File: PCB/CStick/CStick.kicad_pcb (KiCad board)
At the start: 2 copper layers, 39.1 x 31.5 mm, 6 parts, among them J1 Conn_01x04_Male, U1 Stickbox_Assembly

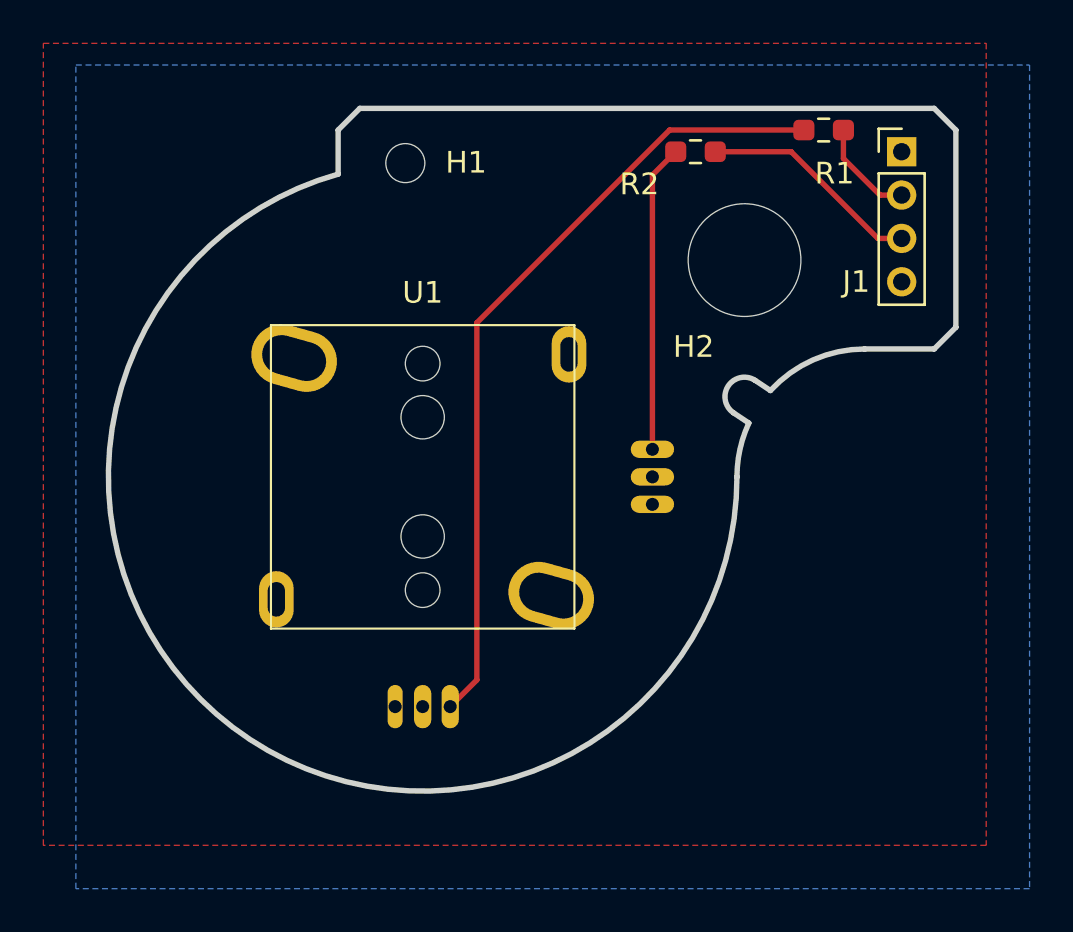
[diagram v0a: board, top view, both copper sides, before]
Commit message: Updated the c-stick board, connector was flipped
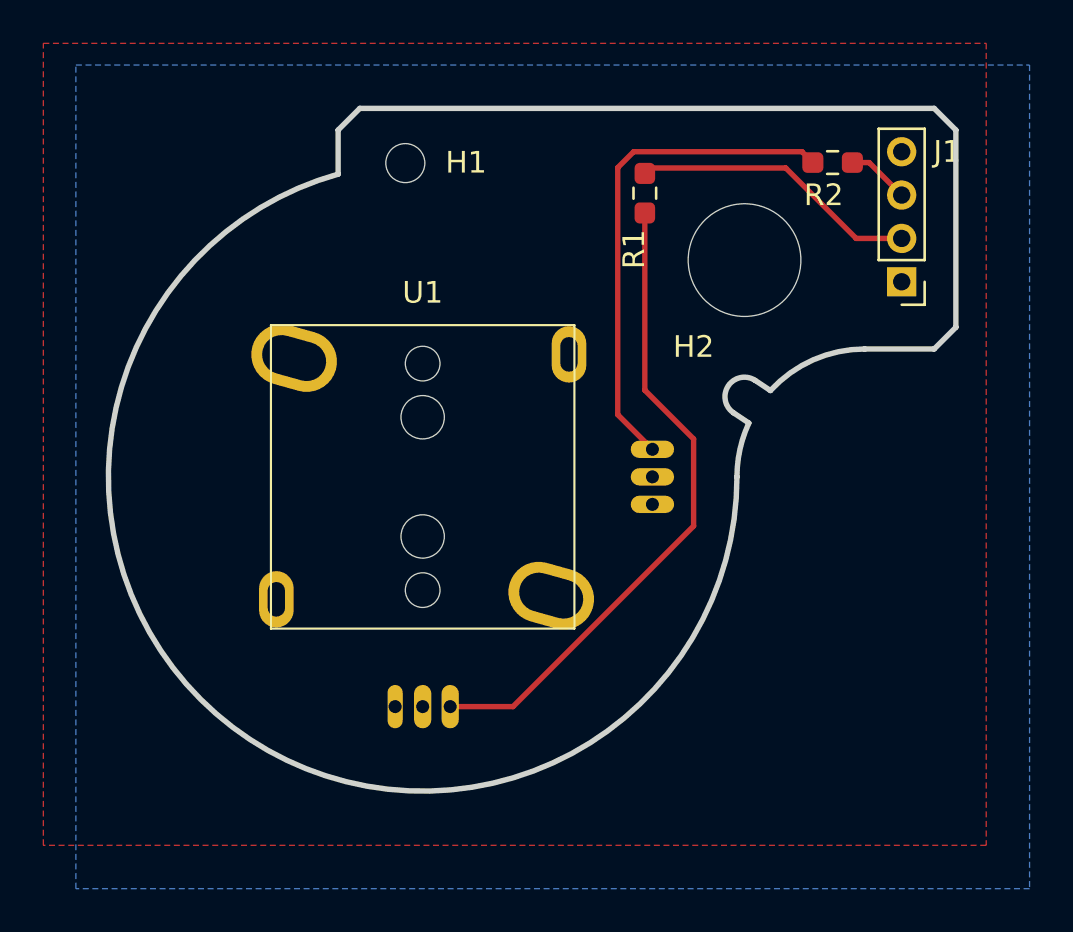
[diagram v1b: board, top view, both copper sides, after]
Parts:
- moved R1 8.75 mm to (160.2, 86.9), turned to -90 degrees
- moved R2 6.34 mm to (168.9, 85.5)
- moved J1 6.00 mm to (172.1, 91.0), turned to 180 degrees
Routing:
- net Net-(R2-Pad2): track 14.2 -> 23.2 mm
- net Net-(J1-Pad2): track 4.70 -> 13.3 mm
- net Net-(J1-Pad3): track 10.3 -> 2.90 mm
- net Net-(R1-Pad2): track 37.0 -> 30.1 mm
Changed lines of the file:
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@@
 (kicad_pcb (version 20211014) (generator pcbnew)
   (general
-    (thickness 1.6)
+    (thickness 1.59)
   )
   (paper "A4")
@@
     (0 "F.Cu" signal)
     (31 "B.Cu" signal)
-    (35 "F.Paste" user)
+    (36 "B.SilkS" user "B.Silkscreen")
     (37 "F.SilkS" user "F.Silkscreen")
+    (38 "B.Mask" user)
     (39 "F.Mask" user)
     (40 "Dwgs.User" user "User.Drawings")
+    (41 "Cmts.User" user "User.Comments")
     (44 "Edge.Cuts" user)
     (45 "Margin" user)
     (46 "B.CrtYd" user "B.Courtyard")
     (47 "F.CrtYd" user "F.Courtyard")
-    (49 "F.Fab" user)
   )
   (setup
@@
       (layer "dielectric 1" (type "core") (thickness 1.51) (material "FR4") (epsilon_r 4.5) (loss_tangent 0.02))
       (layer "B.Cu" (type "copper") (thickness 0.035))
-      (layer "B.Mask" (type "Bottom Solder Mask") (thickness 0.01))
       (copper_finish "None")
       (dielectric_constraints no)
@@
   (net 6 "Net-(R2-Pad2)")
   (footprint "Resistor_SMD:R_0603_1608Metric_Pad0.98x0.95mm_HandSolder" (layer "F.Cu")
-    (at 168.5 84 180)
+    (at 160.25 86.9125 -90)
     (descr "Resistor SMD 0603 (1608 Metric), square (rectangular) end terminal, IPC_7351 nominal with elongated pad for handsoldering. (Body size source: IPC-SM-782 page 72, https://www.pcb-3d.com/wordpress/wp-content/uploads/ipc-sm-782a_amendment_1_and_2.pdf), generated with kicad-footprint-generator")
     (tags "resistor handsolder")
@@
     (property "Sheetname" "")
     (attr smd)
-    (fp_text reference "R1" (at -0.5 -2) (layer "F.SilkS")
-      (effects (font (size 1 1) (thickness 0.15)))
-    )
-    (fp_text value "10k" (at 0 1.43) (layer "F.Fab")
-      (effects (font (size 1 1) (thickness 0.15)))
-    )
-    (fp_text user "${REFERENCE}" (at 0 0) (layer "F.Fab")
+    (fp_text reference "R1" (at 2.5875 0.5 90) (layer "F.SilkS")
+      (effects (font (size 1 1) (thickness 0.15)))
+    )
+    (fp_text value "10k" (at 0 1.43 90) (layer "F.Fab")
+      (effects (font (size 1 1) (thickness 0.15)))
+    )
+    (fp_text user "${REFERENCE}" (at 0 0 90) (layer "F.Fab")
       (effects (font (size 0.4 0.4) (thickness 0.06)))
     )
@@
     (fp_line (start -0.8 0.4125) (end -0.8 -0.4125) (layer "F.Fab") (width 0.1))
     (fp_line (start 0.8 -0.4125) (end 0.8 0.4125) (layer "F.Fab") (width 0.1))
-    (pad "1" smd roundrect (at -0.9125 0 180) (size 0.975 0.95) (layers "F.Cu" "F.Paste" "F.Mask") (roundrect_rratio 0.25)
+    (pad "1" smd roundrect (at -0.9125 0 270) (size 0.975 0.95) (layers "F.Cu" "F.Paste" "F.Mask") (roundrect_rratio 0.25)
       (net 3 "Net-(J1-Pad2)") (pintype "passive"))
-    (pad "2" smd roundrect (at 0.9125 0 180) (size 0.975 0.95) (layers "F.Cu" "F.Paste" "F.Mask") (roundrect_rratio 0.25)
+    (pad "2" smd roundrect (at 0.9125 0 270) (size 0.975 0.95) (layers "F.Cu" "F.Paste" "F.Mask") (roundrect_rratio 0.25)
       (net 5 "Net-(R1-Pad2)") (pintype "passive"))
     (model "${KICAD6_3DMODEL_DIR}/Resistor_SMD.3dshapes/R_0603_1608Metric.wrl"
@@
   )
   (footprint "Resistor_SMD:R_0603_1608Metric_Pad0.98x0.95mm_HandSolder" (layer "F.Cu")
-    (at 162.5875 85 180)
+    (at 168.9125 85.5 180)
     (descr "Resistor SMD 0603 (1608 Metric), square (rectangular) end terminal, IPC_7351 nominal with elongated pad for handsoldering. (Body size source: IPC-SM-782 page 72, https://www.pcb-3d.com/wordpress/wp-content/uploads/ipc-sm-782a_amendment_1_and_2.pdf), generated with kicad-footprint-generator")
     (tags "resistor handsolder")
@@
     (property "Sheetname" "")
     (attr smd)
-    (fp_text reference "R2" (at 2.5875 -1.5) (layer "F.SilkS")
+    (fp_text reference "R2" (at 0.4125 -1.5) (layer "F.SilkS")
       (effects (font (size 1 1) (thickness 0.15)))
     )
@@
   )
   (footprint "Connector_PinHeader_2.00mm:PinHeader_1x04_P2.00mm_Vertical" (layer "F.Cu")
-    (at 172.1 85)
+    (at 172.1 91 180)
     (descr "Through hole straight pin header, 1x04, 2.00mm pitch, single row")
     (tags "Through hole pin header THT 1x04 2.00mm single row")
@@
     (fp_line (start -0.5 -1) (end 1 -1) (layer "F.Fab") (width 0.1))
     (fp_line (start -1 -0.5) (end -0.5 -1) (layer "F.Fab") (width 0.1))
-    (pad "1" thru_hole rect (at 0 0) (size 1.35 1.35) (drill 0.8) (layers *.Cu *.Mask)
+    (pad "1" thru_hole rect (at 0 0 180) (size 1.35 1.35) (drill 0.8) (layers *.Cu *.Mask)
       (net 1 "VCC") (pinfunction "Pin_1") (pintype "passive"))
-    (pad "2" thru_hole oval (at 0 2) (size 1.35 1.35) (drill 0.8) (layers *.Cu *.Mask)
+    (pad "2" thru_hole oval (at 0 2 180) (size 1.35 1.35) (drill 0.8) (layers *.Cu *.Mask)
       (net 3 "Net-(J1-Pad2)") (pinfunction "Pin_2") (pintype "passive"))
-    (pad "3" thru_hole oval (at 0 4) (size 1.35 1.35) (drill 0.8) (layers *.Cu *.Mask)
+    (pad "3" thru_hole oval (at 0 4 180) (size 1.35 1.35) (drill 0.8) (layers *.Cu *.Mask)
       (net 4 "Net-(J1-Pad3)") (pinfunction "Pin_3") (pintype "passive"))
-    (pad "4" thru_hole oval (at 0 6) (size 1.35 1.35) (drill 0.8) (layers *.Cu *.Mask)
+    (pad "4" thru_hole oval (at 0 6 180) (size 1.35 1.35) (drill 0.8) (layers *.Cu *.Mask)
       (net 2 "GND") (pinfunction "Pin_4") (pintype "passive"))
     (model "${KICAD6_3DMODEL_DIR}/Connector_PinHeader_2.00mm.3dshapes/PinHeader_1x04_P2.00mm_Vertical.wrl"
@@
   (gr_line (start 146.1 84) (end 146.1 86.034328) (layer "Edge.Cuts") (width 0.25))
   (gr_line (start 174.6 93.1) (end 174.6 84) (layer "Edge.Cuts") (width 0.25))
-  (segment (start 171.1 87) (end 169.4125 85.3125) (width 0.25) (layer "F.Cu") (net 3))
-  (segment (start 172.1 87) (end 171.1 87) (width 0.25) (layer "F.Cu") (net 3))
-  (segment (start 169.4125 85.3125) (end 169.4125 84) (width 0.25) (layer "F.Cu") (net 3))
-  (segment (start 172.1 89) (end 171 89) (width 0.25) (layer "F.Cu") (net 4))
-  (segment (start 171 89) (end 167 85) (width 0.25) (layer "F.Cu") (net 4))
-  (segment (start 167 85) (end 163.5 85) (width 0.25) (layer "F.Cu") (net 4))
-  (segment (start 161.392684 84) (end 152.5 92.892684) (width 0.25) (layer "F.Cu") (net 5))
-  (segment (start 152.5 109.37) (end 151.27 110.6) (width 0.25) (layer "F.Cu") (net 5))
-  (segment (start 152.5 92.892684) (end 152.5 109.37) (width 0.25) (layer "F.Cu") (net 5))
-  (segment (start 167.5875 84) (end 161.392684 84) (width 0.25) (layer "F.Cu") (net 5))
-  (segment (start 161.675 85) (end 160.6 86.075) (width 0.25) (layer "F.Cu") (net 6))
-  (segment (start 160.6 86.075) (end 160.6 98.73) (width 0.25) (layer "F.Cu") (net 6))
+  (segment (start 170 89) (end 166.75 85.75) (width 0.25) (layer "F.Cu") (net 3))
+  (segment (start 172.1 89) (end 170 89) (width 0.25) (layer "F.Cu") (net 3))
+  (segment (start 166.75 85.75) (end 160.5 85.75) (width 0.25) (layer "F.Cu") (net 3))
+  (segment (start 160.5 85.75) (end 160.25 86) (width 0.25) (layer "F.Cu") (net 3))
+  (segment (start 170.6 85.5) (end 169.825 85.5) (width 0.25) (layer "F.Cu") (net 4))
+  (segment (start 172.1 87) (end 170.6 85.5) (width 0.25) (layer "F.Cu") (net 4))
+  (segment (start 160.25 96) (end 162.5 98.25) (width 0.25) (layer "F.Cu") (net 5))
+  (segment (start 162.5 98.25) (end 162.5 102.269911) (width 0.25) (layer "F.Cu") (net 5))
+  (segment (start 160.25 87.825) (end 160.25 96) (width 0.25) (layer "F.Cu") (net 5))
+  (segment (start 154.169911 110.6) (end 151.27 110.6) (width 0.25) (layer "F.Cu") (net 5))
+  (segment (start 162.5 102.269911) (end 154.169911 110.6) (width 0.25) (layer "F.Cu") (net 5))
+  (segment (start 159 97.13) (end 160.6 98.73) (width 0.25) (layer "F.Cu") (net 6))
+  (segment (start 167.5 85) (end 159.733842 85) (width 0.25) (layer "F.Cu") (net 6))
+  (segment (start 159 85.733842) (end 159 97.13) (width 0.25) (layer "F.Cu") (net 6))
+  (segment (start 159.733842 85) (end 159 85.733842) (width 0.25) (layer "F.Cu") (net 6))
+  (segment (start 168 85.5) (end 167.5 85) (width 0.25) (layer "F.Cu") (net 6))
   (zone (net 1) (net_name "VCC") (layer "F.Cu") (hatch edge 0.508)
     (connect_pads (clearance 0.508))
